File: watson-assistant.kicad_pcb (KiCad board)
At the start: 4 copper layers, 65 x 56 mm, 44 parts, among them J3 40HAT, J6 CONN_02X02, J9 CONN_01X02, Q1 DMG2305UX, Q2 DMMT5401, Q3 ELECTRET, U1 WM8731, U2 CAT24C32, U3 SN74AHCT125

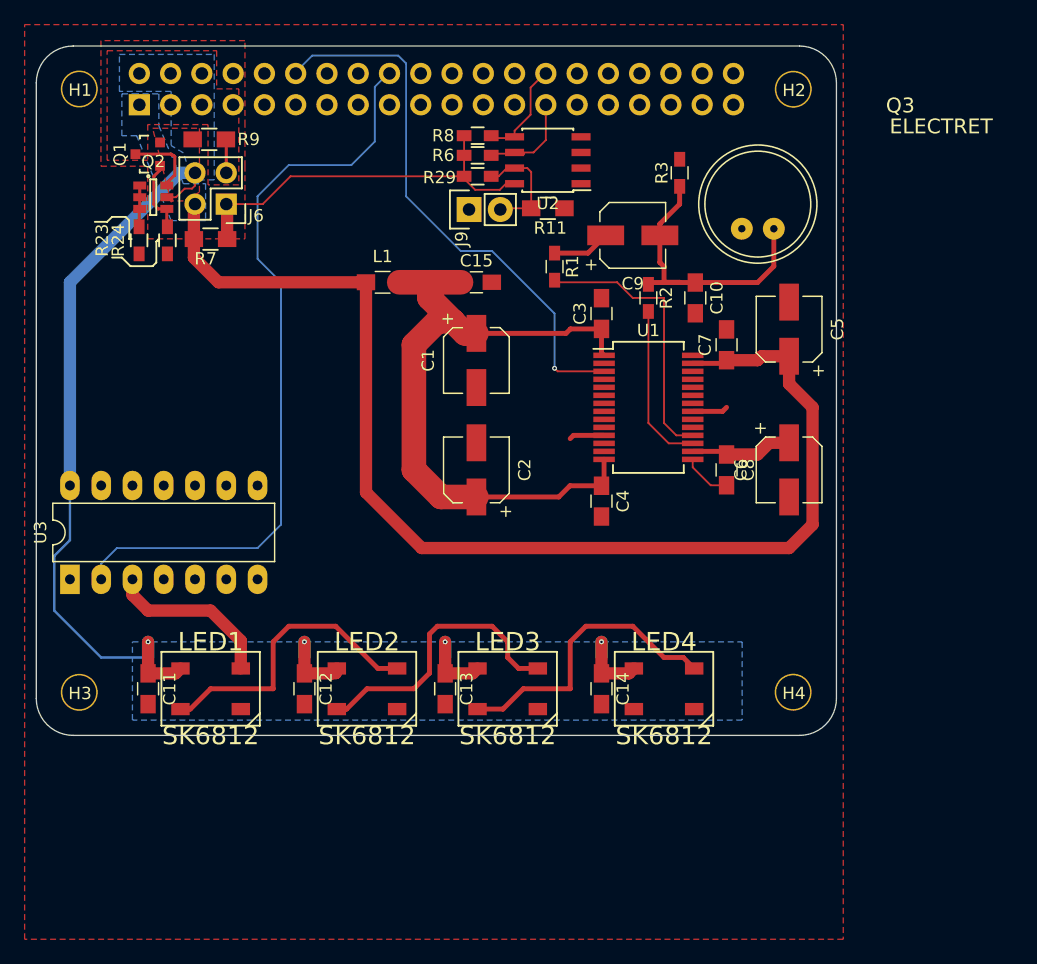
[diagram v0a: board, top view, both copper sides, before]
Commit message: First version with all pcb nets connected
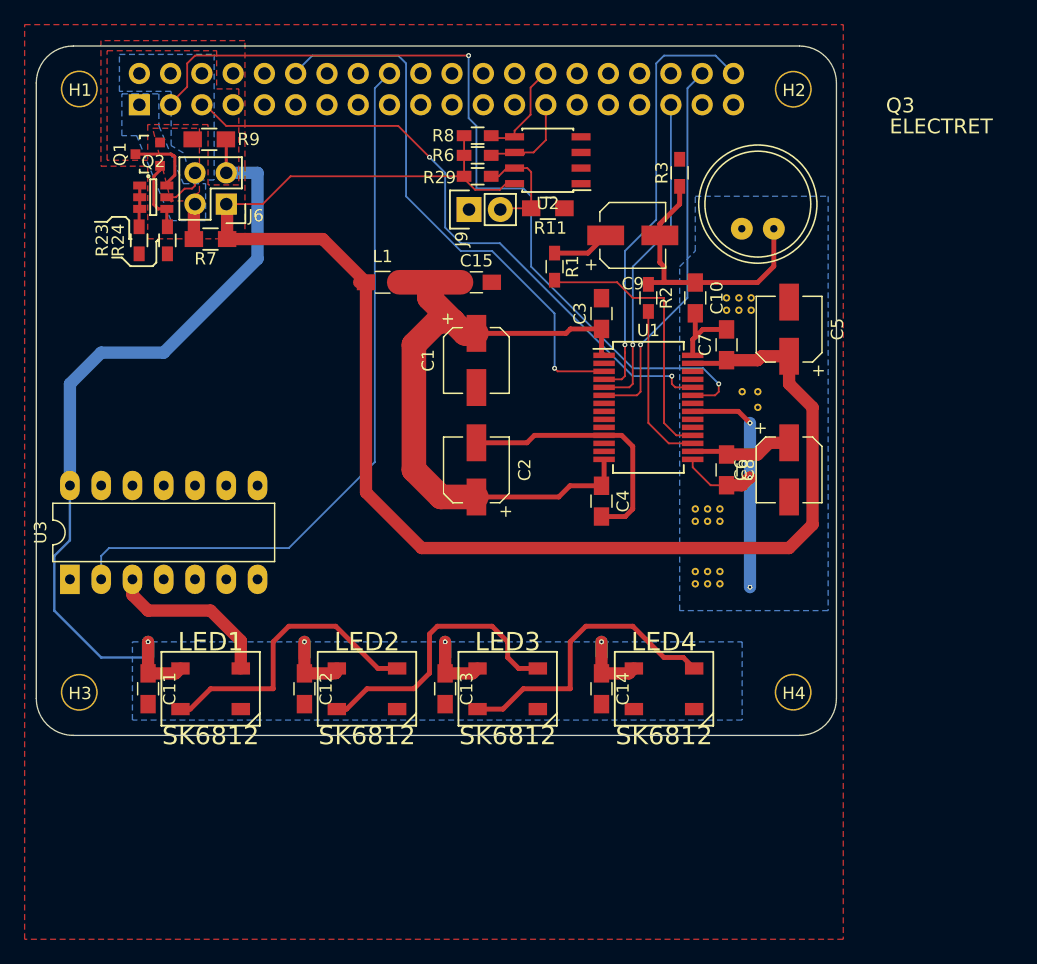
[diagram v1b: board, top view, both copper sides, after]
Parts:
- added REF**: VIA-0.6mm, project_footprints:VIA-0.6mm, F.Cu at (136.6, 82.3)
- added REF**: VIA-0.6mm, project_footprints:VIA-0.6mm, F.Cu at (134.1, 99.4)
- added REF**: VIA-0.6mm, project_footprints:VIA-0.6mm, F.Cu at (133.1, 99.4)
- added REF**: VIA-0.6mm, project_footprints:VIA-0.6mm, F.Cu at (132.1, 99.4)
- added REF**: VIA-0.6mm, project_footprints:VIA-0.6mm, F.Cu at (134.1, 98.4)
- added REF**: VIA-0.6mm, project_footprints:VIA-0.6mm, F.Cu at (133.1, 98.4)
- added REF**: VIA-0.6mm, project_footprints:VIA-0.6mm, F.Cu at (132.1, 98.4)
- added REF**: VIA-0.6mm, project_footprints:VIA-0.6mm, F.Cu at (134.1, 104.5)
- added REF**: VIA-0.6mm, project_footprints:VIA-0.6mm, F.Cu at (133.1, 104.5)
- added REF**: VIA-0.6mm, project_footprints:VIA-0.6mm, F.Cu at (132.1, 104.5)
- added REF**: VIA-0.6mm, project_footprints:VIA-0.6mm, F.Cu at (134.1, 103.5)
- added REF**: VIA-0.6mm, project_footprints:VIA-0.6mm, F.Cu at (135.6, 82.3)
- added REF**: VIA-0.6mm, project_footprints:VIA-0.6mm, F.Cu at (133.1, 103.5)
- added REF**: VIA-0.6mm, project_footprints:VIA-0.6mm, F.Cu at (132.1, 103.5)
- added REF**: VIA-0.6mm, project_footprints:VIA-0.6mm, F.Cu at (134.6, 82.3)
- added REF**: VIA-0.6mm, project_footprints:VIA-0.6mm, F.Cu at (136.6, 81.3)
- added REF**: VIA-0.6mm, project_footprints:VIA-0.6mm, F.Cu at (135.6, 81.3)
- added REF**: VIA-0.6mm, project_footprints:VIA-0.6mm, F.Cu at (134.6, 81.3)
- added REF**: VIA-0.6mm, project_footprints:VIA-0.6mm, F.Cu at (137.2, 90.2)
- added REF**: VIA-0.6mm, project_footprints:VIA-0.6mm, F.Cu at (137.2, 88.9)
- added REF**: VIA-0.6mm, project_footprints:VIA-0.6mm, F.Cu at (135.9, 88.9)
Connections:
- J3 pad 1: +3V3 -> /P3V3_HAT
- J3 pad 2: +5V -> /P5V_HAT
- J3 pad 4: +5V -> /P5V_HAT
- J6 pad 1: /P3V3 -> +3V3
- J6 pad 2: +3V3 -> /P3V3_HAT
- J6 pad 3: /P5V -> +5V
- J6 pad 4: +5V -> /P5V_HAT
- Q1 pad 2: +5V -> /P5V_HAT
- Q1 pad 3: /P5V -> +5V
- Q2 pad 5: +5V -> /P5V_HAT
- Q2 pad 6: /P5V -> +5V
- R29 pad 1: /P3V3 -> +3V3
- R6 pad 1: /P3V3 -> +3V3
- R7 pad 1: +3V3 -> /P3V3_HAT
- R7 pad 2: /P3V3 -> +3V3
- R8 pad 1: /P3V3 -> +3V3
- R9 pad 1: +5V -> /P5V_HAT
- R9 pad 2: /P5V -> +5V
- U2 pad 8: /P3V3 -> +3V3
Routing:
- net /SDA: track 0.00 -> 70.6 mm, vias 0 -> 2
- net /SCL: track 0.00 -> 52.4 mm, vias 0 -> 2
- net GND: track 9.74 -> 52.0 mm, vias 0 -> 3
- net /A_DOUT: track 0.00 -> 35.4 mm, vias 0 -> 1
- net /P3V3: track 31.3 -> 0.00 mm
- net /A_DIN: track 0.00 -> 31.0 mm, vias 0 -> 1
- net /LR_CLK: track 0.00 -> 26.4 mm, vias 0 -> 1
- net +3V3: track 97.7 -> 123.1 mm
- net +5V: track 80.7 -> 93.3 mm
- net /P5V: track 9.02 -> 0.00 mm
- net /P5V_HAT: track 0.00 -> 3.77 mm
- net /P3V3_HAT: track 0.00 -> 2.88 mm
- net /GPIO18: track 62.1 -> 59.5 mm
- added copper zone on F.Cu, net +5V
- added copper zone on B.Cu, net GND
- removed copper zone on F.Cu, net /P5V

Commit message: Add silk screen logos
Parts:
- added REF***: OSHW-Logo_7.5x8mm_SilkScreen, Symbols:OSHW-Logo_7.5x8mm_SilkScreen, F.Cu at (103.5, 102.9)
- added REF***: KiCad-Logo2_6mm_SilkScreen, Symbols:KiCad-Logo2_6mm_SilkScreen, F.Cu at (88.9, 91.4)

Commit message: Add terminal for speaker output
This adds a terminal for a speaker. None of the commonly available pcb
mount speakers fit on the hat board with all the other components, so
this adds a terminal on the left edge to wire a speaker to.
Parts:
- added LS1: Speaker, Connectors_Terminal_Blocks:TerminalBlock_Pheonix_PT-3.5mm_2pol, F.Cu at (83.8, 87.0)
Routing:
- net /L_OUT: track 0.00 -> 64.1 mm, vias 0 -> 4
- net +5V: track 93.3 -> 96.4 mm
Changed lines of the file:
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@@
 (kicad_pcb (version 4) (host pcbnew 4.0.6)
   (general
-    (links 128)
+    (links 130)
     (no_connects 0)
-    (area 71.978573 45.025 229.685714 133.380001)
+    (area 78.496355 60.76761 143.596357 116.867612)
     (thickness 1.6)
     (drawings 67)
-    (tracks 303)
+    (tracks 319)
     (zones 0)
-    (modules 67)
+    (modules 68)
     (nets 71)
   )
@@
   )
   (setup
-    (last_trace_width 0.15)
+    (last_trace_width 0.4)
     (user_trace_width 0.15)
     (user_trace_width 0.2)
@@
       (xy -2.537313 -2.939947) (xy -2.454562 -2.96715) (xy -2.376928 -2.977424) (xy -2.273043 -2.973429)) (layer F.SilkS) (width 0.01))
   )
+  (module Connectors_Terminal_Blocks:TerminalBlock_Pheonix_PT-3.5mm_2pol (layer F.Cu)
+    (at 83.82 86.995 90)
+    (descr "2-way 3.5mm pitch terminal block, Phoenix PT series")
+    (fp_text reference LS1 (at 1.75 -4.3 90) (layer F.SilkS)
+      (effects (font (size 1 1) (thickness 0.15)))
+    )
+    (fp_text value Speaker (at 1.75 6 90) (layer F.Fab)
+      (effects (font (size 1 1) (thickness 0.15)))
+    )
+    (fp_line (start -1.9 -3.3) (end 5.4 -3.3) (layer F.CrtYd) (width 0.05))
+    (fp_line (start -1.9 4.7) (end -1.9 -3.3) (layer F.CrtYd) (width 0.05))
+    (fp_line (start 5.4 4.7) (end -1.9 4.7) (layer F.CrtYd) (width 0.05))
+    (fp_line (start 5.4 -3.3) (end 5.4 4.7) (layer F.CrtYd) (width 0.05))
+    (fp_line (start 1.75 4.1) (end 1.75 4.5) (layer F.SilkS) (width 0.15))
+    (fp_line (start -1.75 3) (end 5.25 3) (layer F.SilkS) (width 0.15))
+    (fp_line (start -1.75 4.1) (end 5.25 4.1) (layer F.SilkS) (width 0.15))
+    (fp_line (start -1.75 -3.1) (end -1.75 4.5) (layer F.SilkS) (width 0.15))
+    (fp_line (start 5.25 4.5) (end 5.25 -3.1) (layer F.SilkS) (width 0.15))
+    (fp_line (start 5.25 -3.1) (end -1.75 -3.1) (layer F.SilkS) (width 0.15))
+    (pad 2 thru_hole circle (at 3.5 0 90) (size 2.4 2.4) (drill 1.2) (layers *.Cu *.Mask)
+      (net 1 GND))
+    (pad 1 thru_hole rect (at 0 0 90) (size 2.4 2.4) (drill 1.2) (layers *.Cu *.Mask)
+      (net 52 /L_OUT))
+    (model Terminal_Blocks.3dshapes/TerminalBlock_Pheonix_PT-3.5mm_2pol.wrl
+      (at (xyz 0 0 0))
+      (scale (xyz 1 1 1))
+      (rotate (xyz 0 0 0))
+    )
+  )
   (gr_text "If you want to use an SMT 40-pin header, please move the top edge up \nby 0.5mm and locate the header in the same location as the current TH part." (at 117.3 47.5) (layer Cmts.User)
     (effects (font (size 1.5 1.5) (thickness 0.3)))
@@
   (segment (start 137.14 80.03) (end 132.08 80.03) (width 0.4) (layer F.Cu) (net 13))
   (segment (start 138.46 78.71) (end 137.14 80.03) (width 0.4) (layer F.Cu) (net 13))
-  (segment (start 93.98 71.12) (end 96.52 71.12) (width 1) (layer B.Cu) (net 14))
-  (segment (start 96.52 71.12) (end 96.52 78.105) (width 1) (layer B.Cu) (net 14))
-  (segment (start 96.52 78.105) (end 88.9 85.725) (width 1) (layer B.Cu) (net 14))
-  (segment (start 88.9 85.725) (end 83.82 85.725) (width 1) (layer B.Cu) (net 14))
-  (segment (start 83.82 85.725) (end 81.28 88.265) (width 1) (layer B.Cu) (net 14))
-  (segment (start 81.28 88.265) (end 81.28 96.52) (width 1) (layer B.Cu) (net 14))
+  (segment (start 93.98 71.12) (end 95.885 71.12) (width 1) (layer B.Cu) (net 14) (status 400000))
+  (segment (start 81.28 94.615) (end 81.28 96.52) (width 1) (layer B.Cu) (net 14) (status 800000))
+  (segment (start 82.55 93.345) (end 81.28 94.615) (width 1) (layer B.Cu) (net 14))
+  (segment (start 92.71 93.345) (end 82.55 93.345) (width 1) (layer B.Cu) (net 14))
+  (segment (start 97.155 88.9) (end 92.71 93.345) (width 1) (layer B.Cu) (net 14))
+  (segment (start 97.155 72.39) (end 97.155 88.9) (width 1) (layer B.Cu) (net 14))
+  (segment (start 95.885 71.12) (end 97.155 72.39) (width 1) (layer B.Cu) (net 14))
   (segment (start 93.95 68.4) (end 93.95 67.915) (width 0.2) (layer F.Cu) (net 14))
   (segment (start 93.98 71.12) (end 93.98 68.43) (width 0.25) (layer F.Cu) (net 14) (status 30))
@@
   (segment (start 89.15 71.95) (end 89.15 72.15) (width 0.25) (layer F.Cu) (net 14) (status 30))
   (segment (start 81.28 96.52) (end 81.28 100.965) (width 0.2) (layer B.Cu) (net 14))
-  (segment (start 81.28 100.965) (end 80.01 102.235) (width 0.2) (layer B.Cu) (net 14))
-  (segment (start 80.01 102.235) (end 80.01 106.68) (width 0.2) (layer B.Cu) (net 14))
-  (segment (start 80.01 106.68) (end 83.82 110.49) (width 0.2) (layer B.Cu) (net 14))
-  (segment (start 83.82 110.49) (end 87.63 110.49) (width 0.2) (layer B.Cu) (net 14))
-  (segment (start 87.63 109.22) (end 87.63 111.78) (width 1) (layer F.Cu) (net 14))
-  (segment (start 87.63 109.22) (end 87.63 110.49) (width 1) (layer B.Cu) (net 14))
   (via (at 87.63 109.22) (size 0.4) (drill 0.2) (layers F.Cu B.Cu) (net 14))
+  (segment (start 87.63 109.22) (end 87.63 110.49) (width 1) (layer B.Cu) (net 14))
+  (segment (start 87.63 109.22) (end 87.63 111.78) (width 1) (layer F.Cu) (net 14))
+  (segment (start 83.82 110.49) (end 87.63 110.49) (width 0.2) (layer B.Cu) (net 14))
+  (segment (start 80.01 106.68) (end 83.82 110.49) (width 0.2) (layer B.Cu) (net 14))
+  (segment (start 80.01 102.235) (end 80.01 106.68) (width 0.2) (layer B.Cu) (net 14))
+  (segment (start 81.28 100.965) (end 80.01 102.235) (width 0.2) (layer B.Cu) (net 14))
   (segment (start 124.46 111.78) (end 124.46 109.22) (width 1) (layer F.Cu) (net 14))
   (segment (start 124.46 109.22) (end 124.46 110.49) (width 1) (layer B.Cu) (net 14))
@@
   (segment (start 129.925 93.095) (end 131.87 93.095) (width 0.15) (layer F.Cu) (net 48))
   (segment (start 128.27 91.44) (end 129.925 93.095) (width 0.15) (layer F.Cu) (net 48))
+  (segment (start 124.67 91.145) (end 118.545 91.145) (width 0.4) (layer F.Cu) (net 52) (status 400000))
+  (segment (start 93.605 86.995) (end 83.82 86.995) (width 0.4) (layer F.Cu) (net 52) (status 800000))
+  (segment (start 98.8 81.8) (end 93.605 86.995) (width 0.4) (layer F.Cu) (net 52))
+  (via (at 98.8 81.8) (size 0.4) (drill 0.2) (layers F.Cu B.Cu) (net 52))
+  (segment (start 98.8 74.6) (end 98.8 81.8) (width 0.4) (layer B.Cu) (net 52))
+  (segment (start 99.4 74) (end 98.8 74.6) (width 0.4) (layer B.Cu) (net 52))
+  (via (at 99.4 74) (size 0.4) (drill 0.2) (layers F.Cu B.Cu) (net 52))
+  (segment (start 106 74) (end 99.4 74) (width 0.4) (layer F.Cu) (net 52))
+  (segment (start 107.4 75.4) (end 106 74) (width 0.4) (layer F.Cu) (net 52))
+  (via (at 107.4 75.4) (size 0.4) (drill 0.2) (layers F.Cu B.Cu) (net 52))
+  (segment (start 107.4 86.6) (end 107.4 75.4) (width 0.4) (layer B.Cu) (net 52))
+  (segment (start 111.6 90.8) (end 107.4 86.6) (width 0.4) (layer B.Cu) (net 52))
+  (via (at 111.6 90.8) (size 0.4) (drill 0.2) (layers F.Cu B.Cu) (net 52))
+  (segment (start 118.2 90.8) (end 111.6 90.8) (width 0.4) (layer F.Cu) (net 52))
+  (segment (start 118.545 91.145) (end 118.2 90.8) (width 0.4) (layer F.Cu) (net 52))
   (zone (net 1) (net_name GND) (layer In2.Cu) (hatch edge 0.508)
     (connect_pads (clearance 0.4))

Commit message: Remove pcb comment about smt header
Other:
- board text removed: "If you want to use an SMT 40-pin header, please move the top edge up by 0.5mm and locate the header in the same location as the current TH part."
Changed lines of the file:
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@@
     (links 130)
     (no_connects 0)
-    (area 78.496355 60.76761 143.596357 116.867612)
+    (area 71.978573 45.025 229.685714 133.380001)
     (thickness 1.6)
-    (drawings 67)
+    (drawings 66)
     (tracks 319)
     (zones 0)
@@
   )
   (setup
-    (last_trace_width 0.4)
+    (last_trace_width 0.15)
     (user_trace_width 0.15)
     (user_trace_width 0.2)
@@
     )
   )
-  (gr_text "If you want to use an SMT 40-pin header, please move the top edge up \nby 0.5mm and locate the header in the same location as the current TH part." (at 117.3 47.5) (layer Cmts.User)
-    (effects (font (size 1.5 1.5) (thickness 0.3)))
-  )
   (gr_text "This is a HAT compatible PCB starting design based on the official\nRaspberry Pi specs at:\nhttps://github.com/raspberrypi/hats/blob/master/designguide.md\n\nCurrently the camera slot and display cutout are not here. \nSee the schematic for the details on the EEPROM and power setup.\n\nThis board does have the correct components for powering the Pi via\nthe HAT. If you need the Pi to provide 5V or 3.3V, please remove or\nconnect the appropriate components." (at 189.4 83.7) (layer Cmts.User)
     (effects (font (size 1.5 1.5) (thickness 0.3)))
@@
   (segment (start 137.14 80.03) (end 132.08 80.03) (width 0.4) (layer F.Cu) (net 13))
   (segment (start 138.46 78.71) (end 137.14 80.03) (width 0.4) (layer F.Cu) (net 13))
-  (segment (start 93.98 71.12) (end 95.885 71.12) (width 1) (layer B.Cu) (net 14) (status 400000))
-  (segment (start 81.28 94.615) (end 81.28 96.52) (width 1) (layer B.Cu) (net 14) (status 800000))
+  (segment (start 93.98 71.12) (end 95.885 71.12) (width 1) (layer B.Cu) (net 14))
+  (segment (start 81.28 94.615) (end 81.28 96.52) (width 1) (layer B.Cu) (net 14))
   (segment (start 82.55 93.345) (end 81.28 94.615) (width 1) (layer B.Cu) (net 14))
   (segment (start 92.71 93.345) (end 82.55 93.345) (width 1) (layer B.Cu) (net 14))
@@
   (segment (start 129.925 93.095) (end 131.87 93.095) (width 0.15) (layer F.Cu) (net 48))
   (segment (start 128.27 91.44) (end 129.925 93.095) (width 0.15) (layer F.Cu) (net 48))
-  (segment (start 124.67 91.145) (end 118.545 91.145) (width 0.4) (layer F.Cu) (net 52) (status 400000))
-  (segment (start 93.605 86.995) (end 83.82 86.995) (width 0.4) (layer F.Cu) (net 52) (status 800000))
+  (segment (start 124.67 91.145) (end 118.545 91.145) (width 0.4) (layer F.Cu) (net 52))
+  (segment (start 93.605 86.995) (end 83.82 86.995) (width 0.4) (layer F.Cu) (net 52))
   (segment (start 98.8 81.8) (end 93.605 86.995) (width 0.4) (layer F.Cu) (net 52))
   (via (at 98.8 81.8) (size 0.4) (drill 0.2) (layers F.Cu B.Cu) (net 52))
